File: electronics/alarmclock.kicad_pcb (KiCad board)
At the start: 2 copper layers, 16 parts, among them J1 SWD, J4 Conn_01x08, J5 Conn_01x08, J6 Barrel_Jack, SW1 Reset, U1 STM32F030C6T6

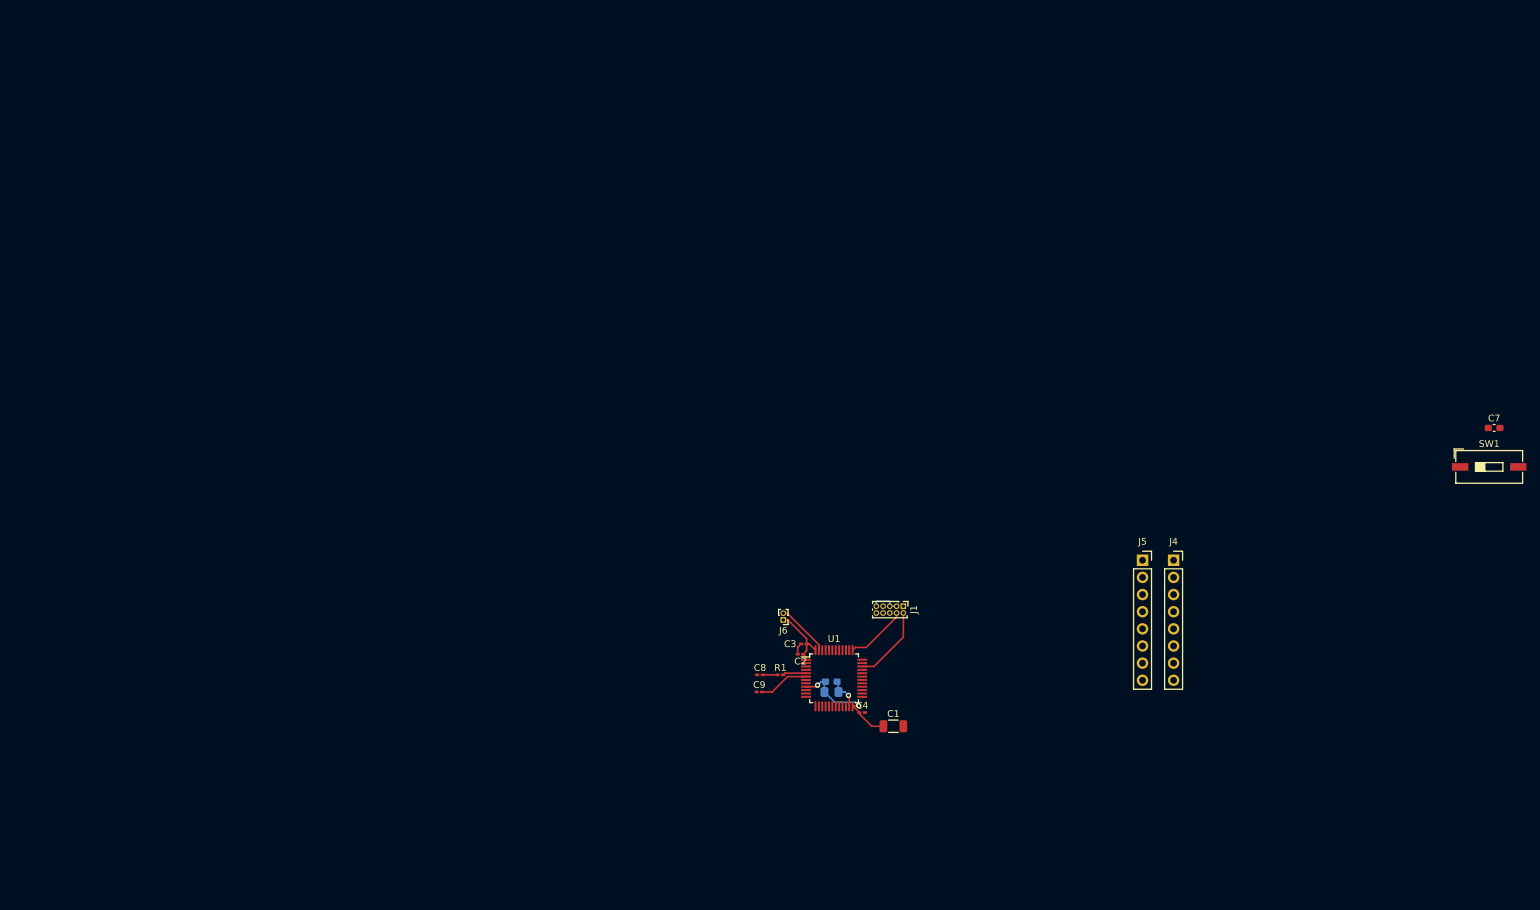
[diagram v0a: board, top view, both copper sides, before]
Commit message: feature: new microprossesor for beter low power performance and smaller footprint
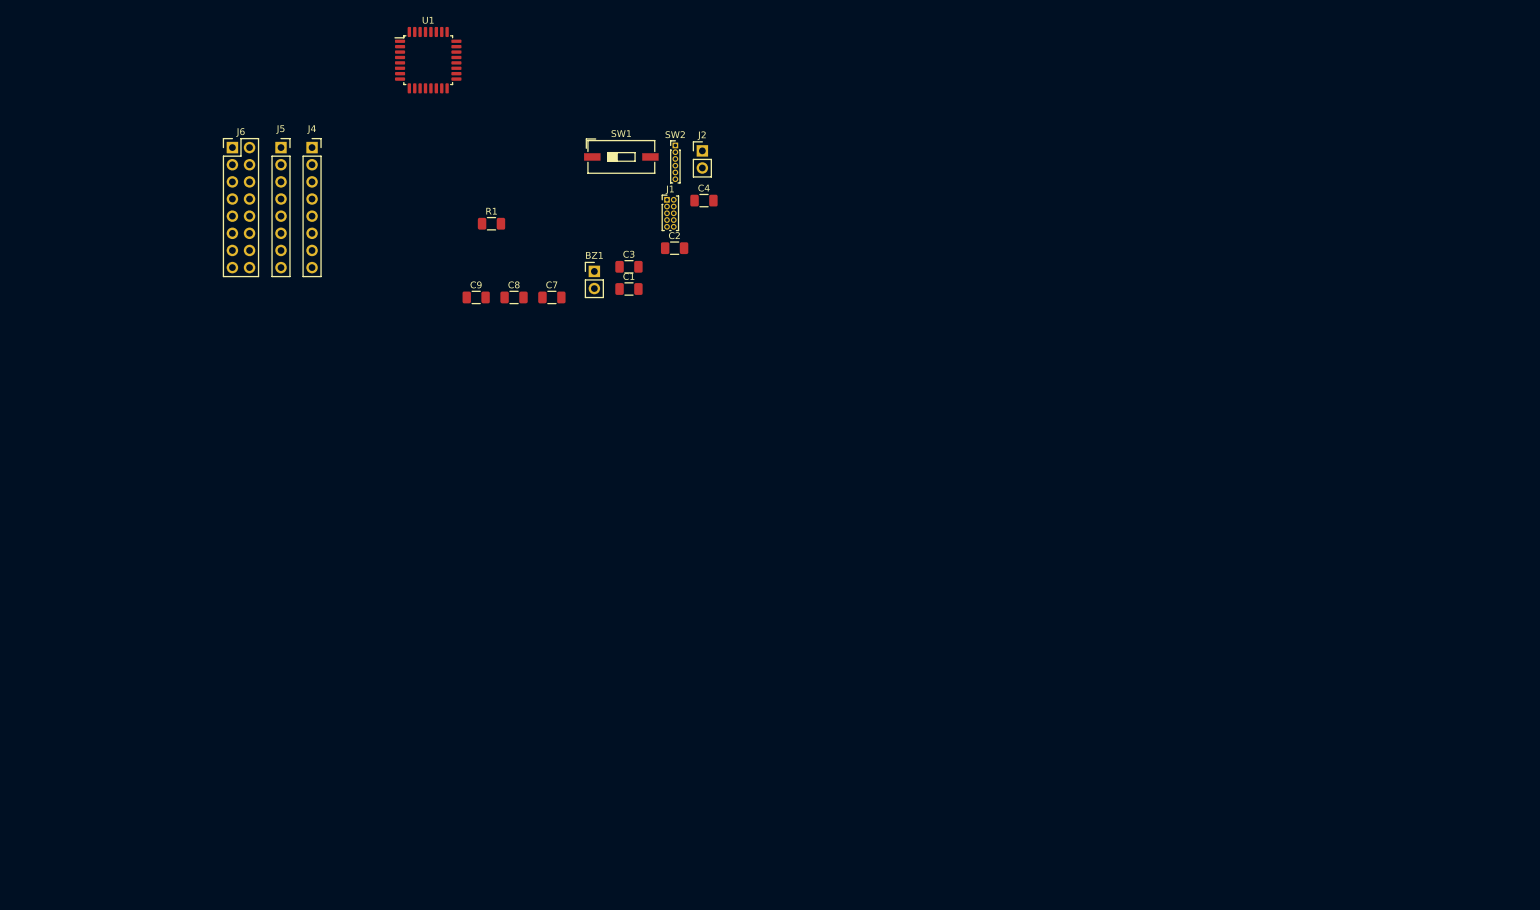
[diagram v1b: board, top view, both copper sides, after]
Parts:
- removed C5: 1uF, Capacitor_SMD:C_0805_2012Metric_Pad1.18x1.45mm_HandSolder
- removed C6: 10nF, Capacitor_SMD:C_0603_1608Metric_Pad1.08x0.95mm_HandSolder
- added BZ1: Buzzer, Connector_PinHeader_2.54mm:PinHeader_1x02_P2.54mm_Vertical, F.Cu at (140.7, 65.2)
- added J2: AudioJack2, Connector_PinHeader_2.54mm:PinHeader_1x02_P2.54mm_Vertical, F.Cu at (156.7, 47.3)
- added SW2: Rotary_Encoder_Switch, Connector_PinHeader_1.00mm:PinHeader_1x06_P1.00mm_Vertical, F.Cu at (152.7, 46.5)
- C2, C3, C4, C8, C9: footprint Capacitor_SMD:C_0201_0603Metric_Pad0.64x0.40mm_HandSolder -> Capacitor_SMD:C_1206_3216Metric
- C7: footprint Capacitor_SMD:C_0603_1608Metric_Pad1.08x0.95mm_HandSolder -> Capacitor_SMD:C_1206_3216Metric
- J6: value Barrel_Jack -> Conn_02x08_Top_Bottom; footprint Connector_PinHeader_1.00mm:PinHeader_1x02_P1.00mm_Vertical -> Connector_PinHeader_2.54mm:PinHeader_2x08_P2.54mm_Vertical
- R1: footprint Resistor_SMD:R_0201_0603Metric_Pad0.64x0.40mm_HandSolder -> Resistor_SMD:R_1206_3216Metric
- U1: value STM32F030C6T6 -> STM32L011K4T6; footprint Package_QFP:LQFP-48_7x7mm_P0.5mm -> Package_QFP:LQFP-32_7x7mm_P0.8mm
- moved J4 141.5 mm to (98.8, 46.9)
- moved J5 141.5 mm to (94.2, 46.9)
- moved C7 140.9 mm to (134.4, 69.1)
- moved SW1 136.5 mm to (144.7, 48.2)
- moved U1 109.5 mm to (116.1, 33.9)
- moved J6 107.5 mm to (87.0, 46.9), turned to 0 degrees
- moved C4 79.4 mm to (156.9, 54.7)
- moved R1 79.4 mm to (125.4, 58.1)
- moved C1 75.7 mm to (145.8, 67.8)
- moved C9 71.9 mm to (123.2, 69.1)
- moved J1 69.7 mm to (151.4, 54.6), turned to 0 degrees
- moved C8 66.7 mm to (128.8, 69.1)
- moved C2 63.0 mm to (152.6, 61.8), turned to 0 degrees
- moved C3 61.6 mm to (145.8, 64.5), turned to 0 degrees
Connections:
- net LED_13 renamed Net-(U1-Pad26)
- net LED_14 renamed Net-(U1-Pad27)
- J6 pad 1: +3V3 -> Net-(J4-Pad1)
- J6 pad 2: GND -> Net-(J4-Pad2)
- U1 pad 10: Alarm -> LED_4
- U1 pad 11: Mute_button -> LED_5
- U1 pad 12: Net-(U1-Pad12) -> LED_6
- U1 pad 13: Net-(U1-Pad13) -> LED_7
- U1 pad 14: Net-(U1-Pad14) -> Alarm
- U1 pad 15: Net-(U1-Pad15) -> Mute_button
- U1 pad 16: Net-(U1-Pad16) -> GND
- U1 pad 17: Net-(U1-Pad17) -> +3V3
- U1 pad 18: LED_0 -> LED_8
- U1 pad 19: LED_1 -> LED_9
- U1 pad 20: LED_2 -> LED_10
- U1 pad 21: LED_10 -> LED_11
- U1 pad 22: LED_11 -> LED_12
- U1 pad 23: GND -> SWDIO
- U1 pad 24: +3V3 -> SWCLK
- U1 pad 25: LED_12 -> LED_15
- U1 pad 28: LED_15 -> Net-(U1-Pad28)
- U1 pad 32: Net-(U1-Pad32) -> GND
- U1 pad 4: Net-(U1-Pad4) -> NRST
- U1 pad 5: OSC_IN -> +3V3
- U1 pad 6: OSC_OUT -> LED_0
- U1 pad 7: NRST -> LED_1
- U1 pad 8: GND -> LED_2
- U1 pad 9: +3V3 -> LED_3
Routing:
- net +3V3: track 28.1 -> 0.00 mm, vias 2 -> 0
- net GND: track 19.0 -> 0.00 mm, vias 1 -> 0
- net SWDIO: track 11.5 -> 0.00 mm
- net SWCLK: track 9.14 -> 0.00 mm
- net OSC_OUT: track 7.45 -> 0.00 mm
- net OSC_IN: track 3.48 -> 0.00 mm
- net Net-(C8-Pad2): track 2.21 -> 0.00 mm

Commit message: added beginning of battery backup
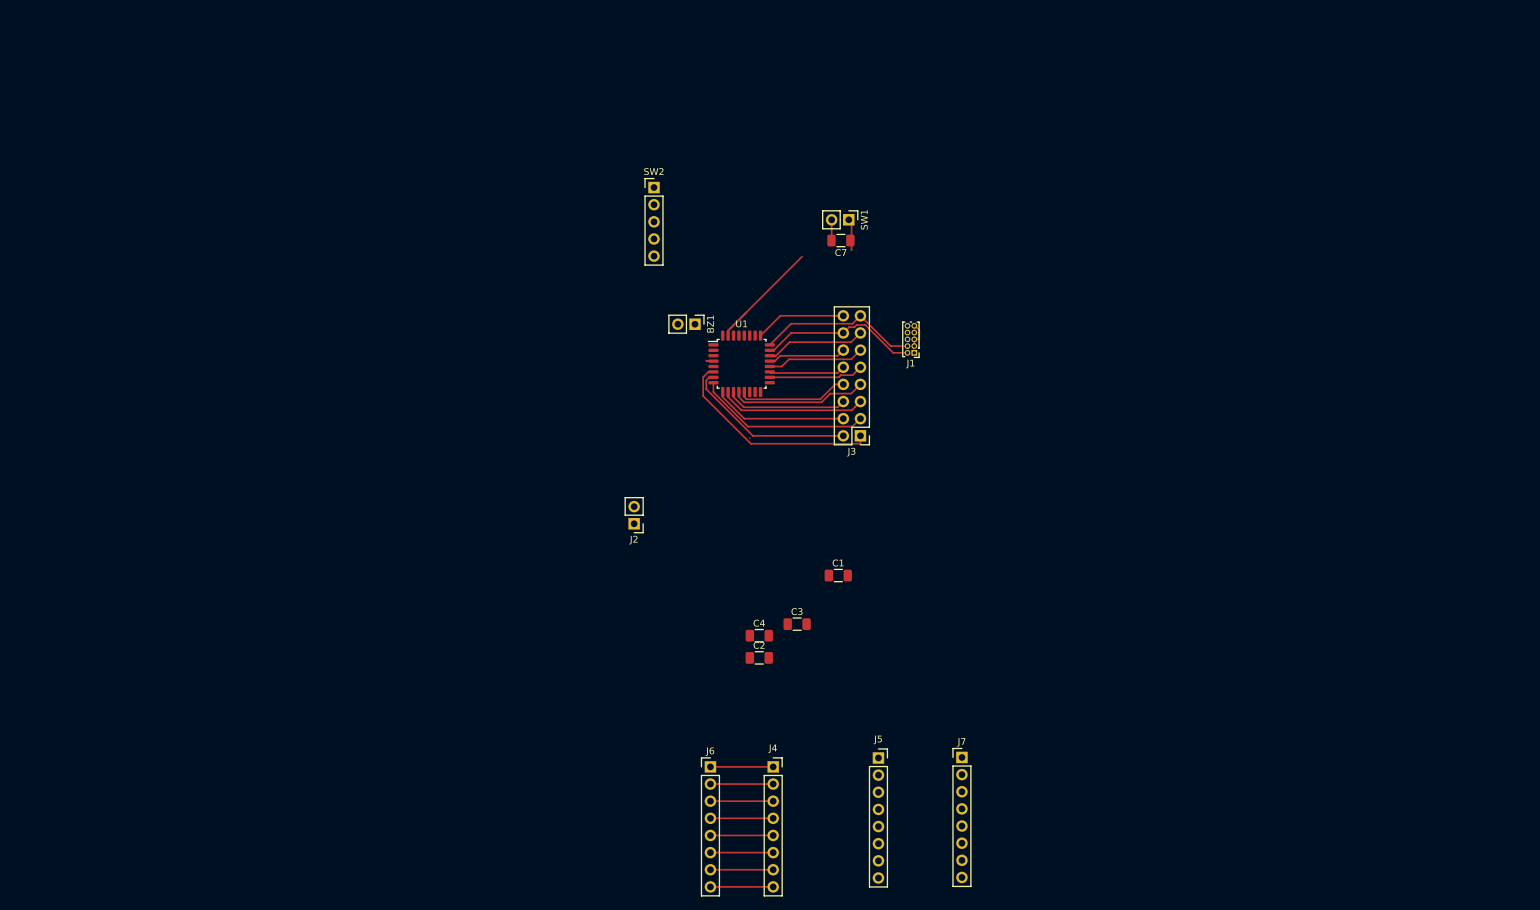
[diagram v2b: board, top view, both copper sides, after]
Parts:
- removed C8, C9: 12pF, Capacitor_SMD:C_1206_3216Metric
- removed R1: 47R, Resistor_SMD:R_1206_3216Metric
- added J3: Conn_02x08_Top_Bottom, Connector_PinHeader_2.54mm:PinHeader_2x08_P2.54mm_Vertical, F.Cu at (180.1, 89.6)
- added J7: PinheaderBottom, Connector_PinHeader_2.54mm:PinHeader_1x08_P2.54mm_Vertical, F.Cu at (195.1, 137.2)
- J4: value Conn_01x08 -> SocketTop
- J5: value Conn_01x08 -> SocketBottom
- J6: value Conn_02x08_Top_Bottom -> PinheaderTop; footprint Connector_PinHeader_2.54mm:PinHeader_2x08_P2.54mm_Vertical -> Connector_PinHeader_2.54mm:PinHeader_1x08_P2.54mm_Vertical
- SW1: footprint Button_Switch_SMD:SW_DIP_SPSTx01_Slide_9.78x4.72mm_W8.61mm_P2.54mm -> Connector_PinHeader_2.54mm:PinHeader_1x02_P2.54mm_Vertical
- SW2: footprint Connector_PinHeader_1.00mm:PinHeader_1x06_P1.00mm_Vertical -> Connector_PinHeader_2.54mm:PinHeader_1x05_P2.54mm_Vertical
- moved J5 126.5 mm to (182.8, 137.3)
- moved J6 115.9 mm to (157.9, 138.6)
- moved J4 114.4 mm to (167.2, 138.6)
- moved C4 65.0 mm to (165.1, 119.2)
- moved U1 64.6 mm to (162.5, 78.9)
- moved C2 62.0 mm to (165.1, 122.5)
- moved C3 58.5 mm to (170.7, 117.5)
- moved J2 56.2 mm to (146.6, 102.6), turned to 180 degrees
- moved C1 52.6 mm to (176.8, 110.3)
- moved C7 43.6 mm to (177.2, 60.6), turned to 180 degrees
- moved J1 43.1 mm to (188.1, 77.3), turned to 180 degrees
- moved SW1 35.0 mm to (178.4, 57.6), turned to 270 degrees
- moved BZ1 16.8 mm to (155.6, 73.0), turned to 270 degrees
- moved SW2 6.99 mm to (149.5, 52.8)
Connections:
- net Net-(U1-Pad29) renamed Rotary_A
- net Net-(U1-Pad30) renamed Rotary_B
- net Net-(U1-Pad31) renamed Switch_Encoder
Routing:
- net LED_0: track 0.00 -> 32.0 mm
- net LED_2: track 0.00 -> 25.8 mm
- net LED_1: track 0.00 -> 25.7 mm
- net SWCLK: track 0.00 -> 24.0 mm
- net SWDIO: track 0.00 -> 23.7 mm
- net LED_4: track 0.00 -> 22.0 mm
- net LED_6: track 0.00 -> 20.2 mm
- net Switch_Encoder: track 0.00 -> 20.1 mm
- net LED_3: track 0.00 -> 19.9 mm
- net LED_5: track 0.00 -> 18.0 mm
- net LED_7: track 0.00 -> 16.5 mm
- net LED_12: track 0.00 -> 14.8 mm
- net LED_10: track 0.00 -> 14.4 mm
- net LED_8: track 0.00 -> 14.0 mm
- net LED_15: track 0.00 -> 13.5 mm
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
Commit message: minor changes
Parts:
- C1, C2, C3, C4: moved to B.Cu
- moved J5 94.9 mm to (248.3, 68.7)
- moved J7 94.9 mm to (260.7, 68.6)
- moved J4 94.9 mm to (232.7, 70.0)
- moved J6 94.9 mm to (223.4, 70.0)
- moved C2 47.6 mm to (153.8, 76.2), turned to 180 degrees
- moved C3 41.3 mm to (153.8, 79.8), turned to 180 degrees
- moved C4 37.3 mm to (170.8, 82.3)
- moved C1 17.6 mm to (169.0, 94.5)
- moved BZ1 1.53 mm to (154.9, 71.6)
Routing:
- net Alarm: track 0.01 -> 15.1 mm, vias 0 -> 1
- net +3V3: track 0.00 -> 9.46 mm, vias 0 -> 3
- net GND: track 7.12 -> 15.3 mm
- net NRST: track 5.75 -> 4.64 mm
